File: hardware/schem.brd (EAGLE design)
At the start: 45.4 x 51.4 mm, 18 parts, among them IC1 7805L, IC2 L298

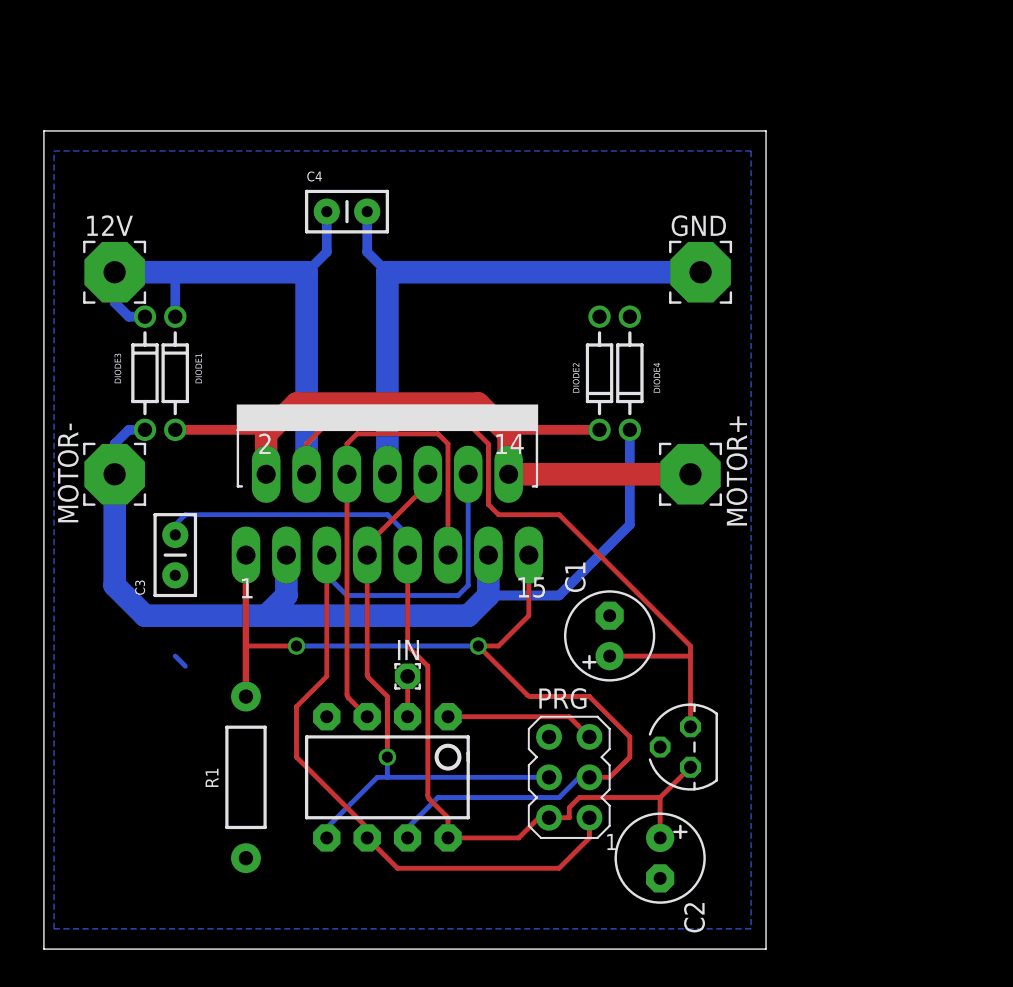
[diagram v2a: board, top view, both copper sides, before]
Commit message: added mounting holes
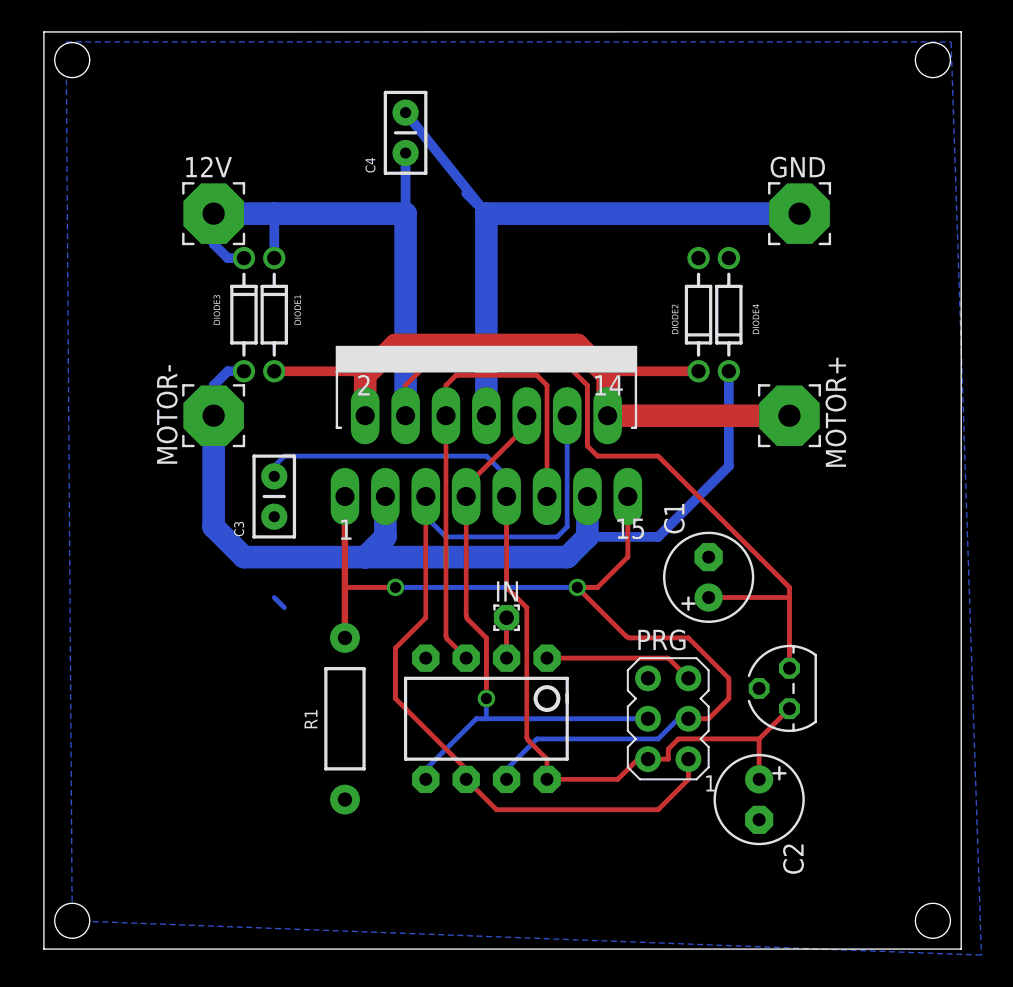
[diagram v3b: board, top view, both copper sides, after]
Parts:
- moved DIODE2 7.23 mm to (41.1, 39.9)
- moved DIODE3 7.23 mm to (12.6, 39.9)
- moved 12V 7.23 mm to (10.7, 46.2)
- moved C1 7.23 mm to (41.8, 23.4)
- moved C2 7.23 mm to (45.0, 9.40)
- moved C3 7.23 mm to (14.5, 27.2)
- moved DIODE1 7.23 mm to (14.5, 39.9)
- moved DIODE4 7.23 mm to (43.1, 39.9)
- moved GND 7.23 mm to (47.5, 46.2)
- moved IC1 7.23 mm to (46.9, 16.4)
- moved IC2 7.23 mm to (27.8, 36.1)
- moved IN 7.23 mm to (29.1, 20.8)
- moved MOTOR+ 7.23 mm to (46.9, 33.5)
- moved MOTOR- 7.23 mm to (10.7, 33.5)
- moved PRG 7.23 mm to (39.2, 14.5)
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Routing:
- net GND: track 37.6 -> 43.2 mm
- net +12V: track 80.8 -> 80.3 mm
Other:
- board size 45.4 x 51.4 mm -> 57.7 x 57.7 mm

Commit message: ground plane and silk screen in prep for fab
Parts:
- moved C4 17.1 mm to (8.13, 41.1), turned to 270 degrees
- turned R1 to 90 degrees
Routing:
- net GND: track 43.2 -> 35.1 mm
- net SCK: track 60.9 -> 62.8 mm, vias 2 -> 0
- net +12V: track 80.3 -> 81.7 mm
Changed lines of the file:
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@@
 <setting verticaltext="up"/>
 </settings>
-<grid distance="0.01" unitdist="inch" unit="inch" style="lines" multiple="1" display="no" altdistance="0.01" altunitdist="inch" altunit="inch"/>
+<grid distance="0.025" unitdist="inch" unit="inch" style="lines" multiple="1" display="no" altdistance="0.025" altunitdist="inch" altunit="inch"/>
 <layers>
 <layer number="1" name="Top" color="4" fill="1" visible="yes" active="yes"/>
@@
 <element name="12V" library="wirepad" package="3,81/1,4" value="" x="10.668" y="46.228"/>
 <element name="GND" library="wirepad" package="3,81/1,4" value="" x="47.498" y="46.228"/>
-<element name="IN" library="wirepad" package="1,6/0,9" value="" x="29.083" y="20.828"/>
+<element name="IN" library="wirepad" package="1,6/0,9" value="" x="29.083" y="20.828" smashed="yes">
+<attribute name="NAME" x="30.226" y="20.574" size="1.27" layer="25" ratio="10"/>
+<attribute name="VALUE" x="29.083" y="21.428" size="0.0254" layer="27"/>
+</element>
 <element name="C1" library="adafruit" package="E2,5-6" value="" x="41.783" y="23.368" rot="R90"/>
 <element name="C2" library="adafruit" package="E2,5-6" value="" x="44.958" y="9.398" rot="R270"/>
@@
 </element>
 <element name="C3" library="SparkFun-Capacitors" package="CAP-PTH-SMALL2" value="100nF" x="14.478" y="27.178" rot="R90"/>
-<element name="C4" library="SparkFun-Capacitors" package="CAP-PTH-SMALL2" value="100nF" x="22.733" y="50.038" rot="R90"/>
-<element name="R1" library="SparkFun-Passives" package="AXIAL-0.4" value="" x="18.923" y="14.478" smashed="yes" rot="R270">
-<attribute name="NAME" x="16.383" y="15.113" size="0.8128" layer="25" font="vector" ratio="15" rot="R270"/>
-<attribute name="VALUE" x="18.542" y="16.764" size="0.8128" layer="21" font="vector" ratio="15" rot="R270"/>
+<element name="C4" library="SparkFun-Capacitors" package="CAP-PTH-SMALL2" value="100nF" x="8.128" y="41.148" smashed="yes" rot="R270">
+<attribute name="NAME" x="4.318" y="42.418" size="0.6096" layer="25" rot="R270"/>
+<attribute name="VALUE" x="5.588" y="42.418" size="0.6096" layer="27" rot="R270"/>
+</element>
+<element name="R1" library="SparkFun-Passives" package="AXIAL-0.4" value="" x="18.923" y="14.478" smashed="yes" rot="R90">
+<attribute name="NAME" x="21.463" y="13.843" size="0.8128" layer="25" font="vector" ratio="15" rot="R90"/>
+<attribute name="VALUE" x="19.304" y="12.192" size="0.8128" layer="21" font="vector" ratio="15" rot="R90"/>
 </element>
 <element name="DIODE1" library="SparkFun-DiscreteSemi" package="DIODE-ZENER" value="DIODE-ZENERPTH" x="14.478" y="39.878" smashed="yes" rot="R270">
@@
 <contactref element="DIODE3" pad="P$1"/>
 <contactref element="DIODE1" pad="P$1"/>
-<wire x1="10.668" y1="46.228" x2="14.478" y2="46.228" width="1.4224" layer="16"/>
+<wire x1="10.668" y1="46.228" x2="12.7" y2="46.228" width="1.4224" layer="16"/>
+<wire x1="12.7" y1="46.228" x2="14.478" y2="46.228" width="1.4224" layer="16"/>
 <wire x1="14.478" y1="46.228" x2="22.733" y2="46.228" width="1.4224" layer="16"/>
 <wire x1="22.733" y1="46.228" x2="22.733" y2="33.528" width="1.4224" layer="16"/>
@@
 <wire x1="46.863" y1="22.098" x2="46.863" y2="17.653" width="0.3048" layer="1"/>
 <wire x1="41.783" y1="22.098" x2="46.863" y2="22.098" width="0.3048" layer="1"/>
-<wire x1="12.573" y1="43.434" x2="11.557" y2="43.434" width="0.6096" layer="16"/>
-<wire x1="11.557" y1="43.434" x2="10.668" y2="44.323" width="0.6096" layer="16"/>
-<wire x1="10.668" y1="44.323" x2="10.668" y2="46.228" width="0.6096" layer="16"/>
 <wire x1="14.478" y1="43.434" x2="14.478" y2="46.228" width="0.6096" layer="16"/>
-<wire x1="22.733" y1="50.038" x2="22.733" y2="46.228" width="0.6096" layer="16"/>
+<wire x1="12.573" y1="43.434" x2="12.573" y2="46.101" width="0.6096" layer="16"/>
+<wire x1="12.573" y1="46.101" x2="12.7" y2="46.228" width="0.6096" layer="16"/>
+<wire x1="8.128" y1="41.148" x2="8.89" y2="41.148" width="0.6096" layer="16"/>
+<wire x1="8.89" y1="41.148" x2="10.668" y2="42.926" width="0.6096" layer="16"/>
+<wire x1="10.668" y1="42.926" x2="10.668" y2="46.228" width="0.6096" layer="16"/>
 </signal>
 <signal name="GND">
@@
 <wire x1="27.813" y1="33.528" x2="27.813" y2="46.228" width="1.4224" layer="16"/>
 <wire x1="27.813" y1="46.228" x2="47.498" y2="46.228" width="1.4224" layer="16"/>
-<wire x1="22.733" y1="52.578" x2="27.813" y2="46.228" width="0.6096" layer="16"/>
 <wire x1="26.543" y1="47.498" x2="27.813" y2="46.228" width="0.6096" layer="16"/>
 <polygon width="0.3048" layer="16" isolate="0.6096">
@@
 <vertex x="58.928" y="-0.381"/>
 <vertex x="1.778" y="1.778"/>
+<vertex x="1.778" y="28.194"/>
+<vertex x="10.668" y="28.194"/>
+<vertex x="10.668" y="32.766"/>
+<vertex x="-0.762" y="32.766"/>
 </polygon>
 <wire x1="14.478" y1="22.098" x2="15.113" y2="21.463" width="0.3048" layer="16"/>
@@
 <wire x1="30.988" y1="13.208" x2="29.083" y2="11.303" width="0.3048" layer="16"/>
 <wire x1="29.083" y1="11.303" x2="29.083" y2="10.668" width="0.3048" layer="16"/>
-<wire x1="40.513" y1="19.558" x2="43.053" y2="17.018" width="0.3048" layer="1"/>
-<wire x1="43.053" y1="17.018" x2="43.053" y2="15.748" width="0.3048" layer="1"/>
-<wire x1="43.053" y1="15.748" x2="41.783" y2="14.478" width="0.3048" layer="1"/>
-<wire x1="41.783" y1="14.478" x2="40.513" y2="14.478" width="0.3048" layer="1"/>
 <contactref element="IC2" pad="1"/>
 <contactref element="IC2" pad="15"/>
 <contactref element="R1" pad="P$1"/>
-<wire x1="18.923" y1="28.448" x2="18.923" y2="22.733" width="0.4064" layer="1"/>
-<wire x1="18.923" y1="22.733" x2="18.923" y2="19.558" width="0.4064" layer="1"/>
-<wire x1="36.703" y1="28.448" x2="36.703" y2="24.638" width="0.3048" layer="1"/>
-<wire x1="36.703" y1="24.638" x2="34.798" y2="22.733" width="0.3048" layer="1"/>
-<via x="33.528" y="22.733" extent="1-16" drill="0.7"/>
-<wire x1="33.528" y1="22.733" x2="22.098" y2="22.733" width="0.3048" layer="16"/>
-<via x="22.098" y="22.733" extent="1-16" drill="0.7"/>
-<wire x1="22.098" y1="22.733" x2="18.923" y2="22.733" width="0.3048" layer="1"/>
-<wire x1="34.798" y1="22.733" x2="33.528" y2="22.733" width="0.3048" layer="1"/>
-<wire x1="40.513" y1="19.558" x2="36.8345125" y2="19.558" width="0.3048" layer="1"/>
-<wire x1="36.8345125" y1="19.558" x2="36.61000625" y2="19.65099375" width="0.3048" layer="1" curve="-45"/>
-<wire x1="36.61000625" y1="19.65099375" x2="33.528" y2="22.733" width="0.3048" layer="1"/>
+<wire x1="36.703" y1="28.448" x2="36.703" y2="24.257" width="0.4064" layer="1"/>
+<wire x1="36.703" y1="24.257" x2="41.91" y2="19.05" width="0.4064" layer="1"/>
+<wire x1="41.91" y1="19.05" x2="41.91" y2="15.875" width="0.4064" layer="1"/>
+<wire x1="41.91" y1="15.875" x2="40.513" y2="14.478" width="0.4064" layer="1"/>
+<wire x1="18.923" y1="28.448" x2="18.923" y2="22.098" width="0.6096" layer="1"/>
+<wire x1="18.923" y1="22.098" x2="16.51" y2="19.685" width="0.6096" layer="1"/>
+<wire x1="16.51" y1="19.685" x2="16.51" y2="11.811" width="0.6096" layer="1"/>
+<wire x1="16.51" y1="11.811" x2="18.923" y2="9.398" width="0.6096" layer="1"/>
+<wire x1="29.083" y1="10.668" x2="26.67" y2="8.255" width="0.4064" layer="16"/>
+<wire x1="26.67" y1="8.255" x2="20.32" y2="8.255" width="0.4064" layer="16"/>
+<wire x1="20.32" y1="8.255" x2="19.177" y2="9.398" width="0.4064" layer="16"/>
+<wire x1="19.177" y1="9.398" x2="18.923" y2="9.398" width="0.4064" layer="16"/>
 </signal>
 <signal name="OUT2">
